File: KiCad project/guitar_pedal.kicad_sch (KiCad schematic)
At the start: 43 parts, among them J1 NMJ6HCD2, J2 NMJ6HCD2, J3 AVR-ISP-6, SW1 SW_SPST, SW2 SWITCH_3PDT, U1 ATmega1284-P, U2 L7805, U3 TL061, U4 TL061, Y1 Crystal 16MHz

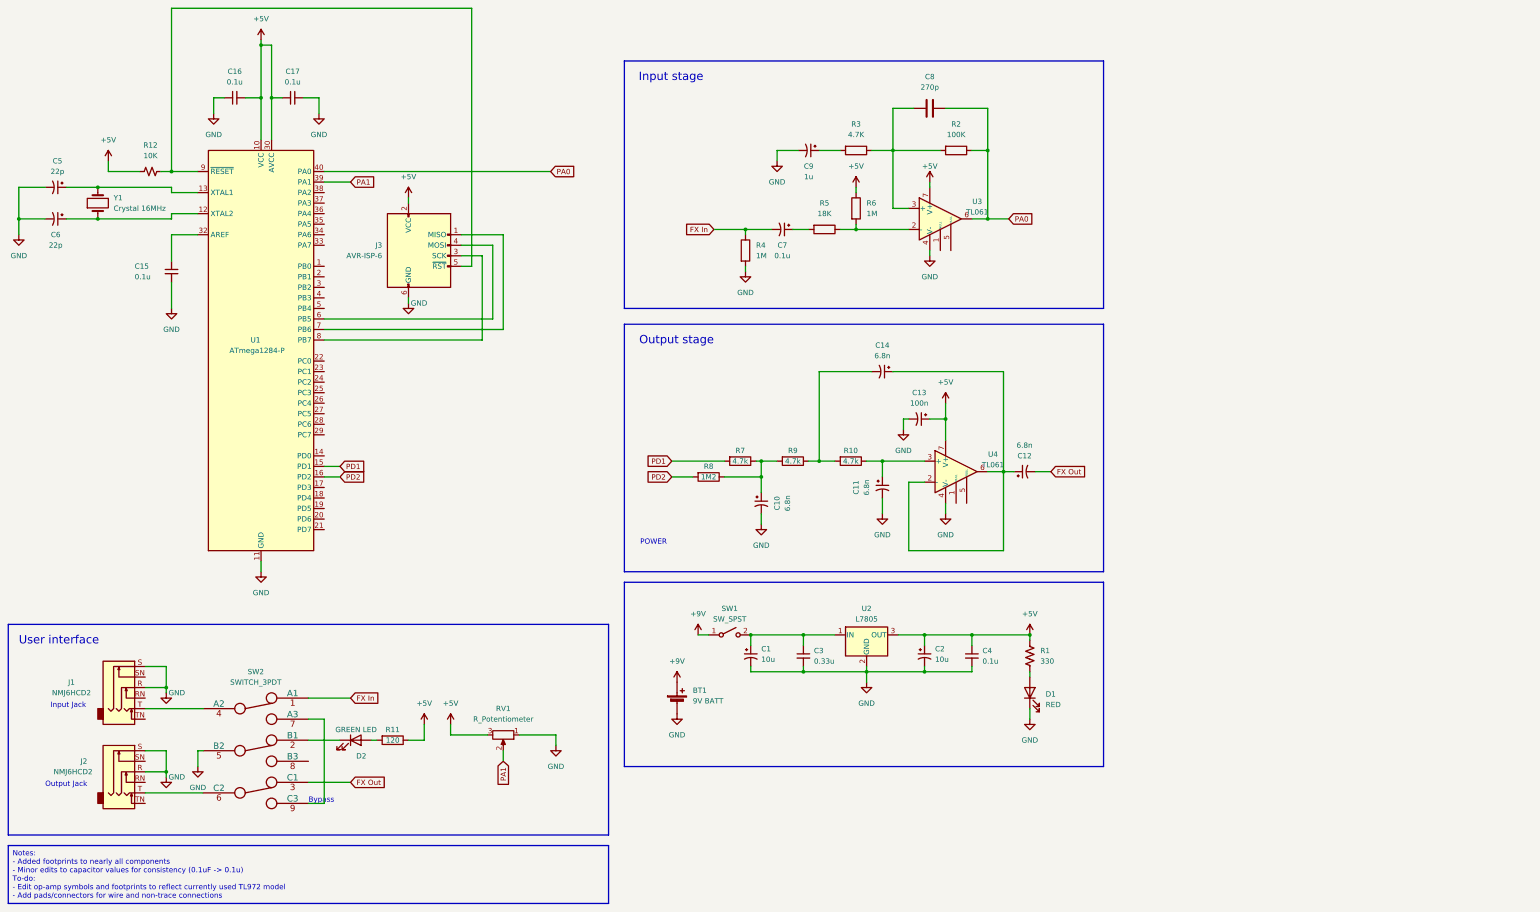
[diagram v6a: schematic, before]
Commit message: Updated schematic to match available components.
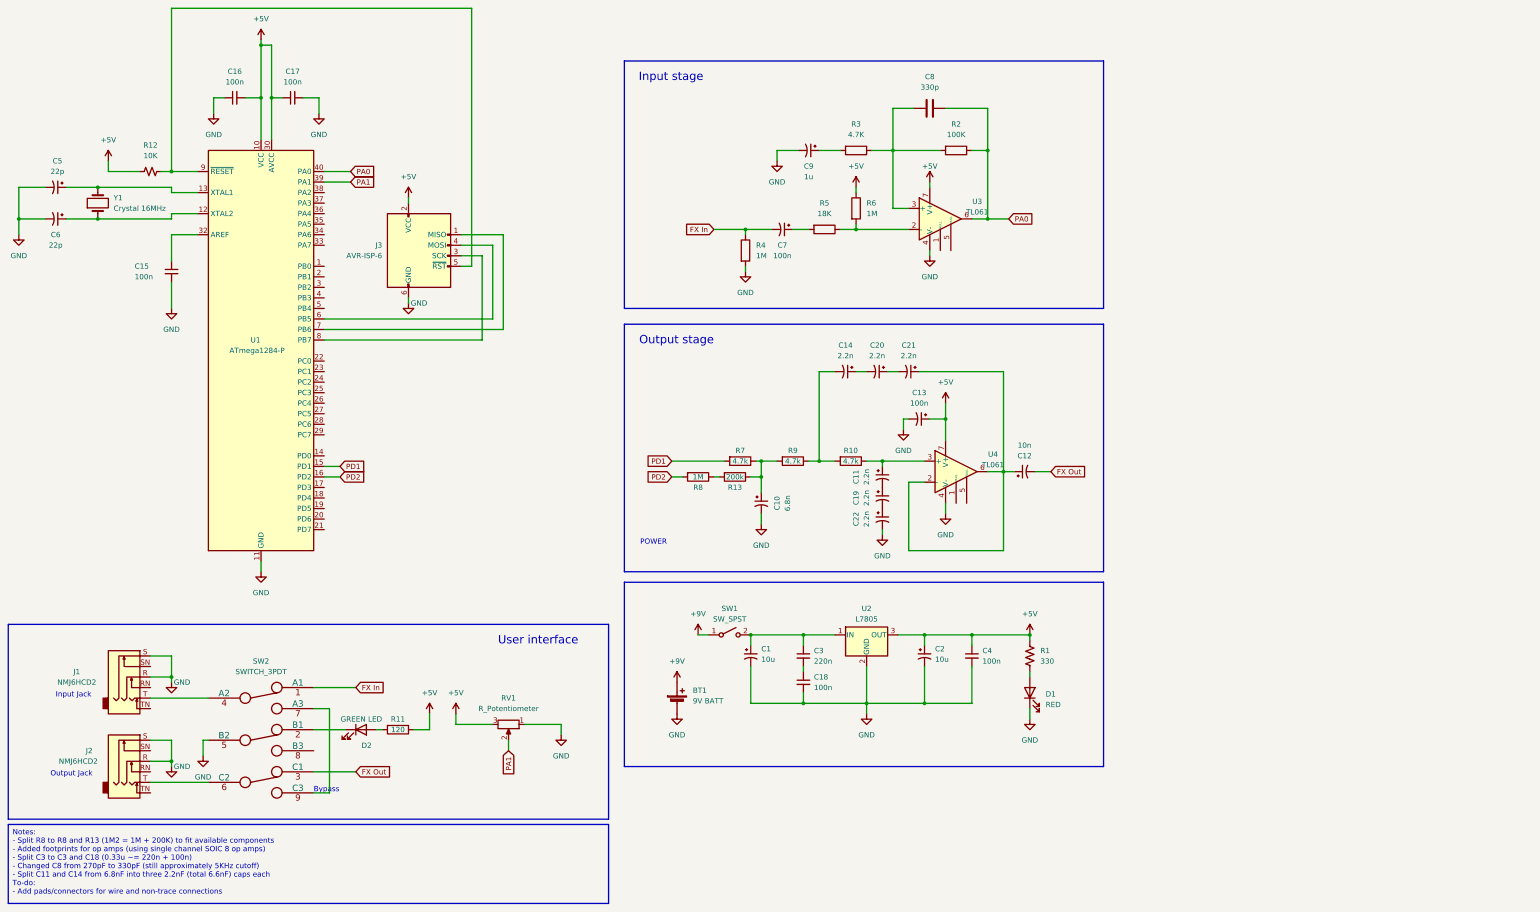
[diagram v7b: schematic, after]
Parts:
- added C18: 100n, Capacitor_SMD:C_1206_3216Metric, symbol Device:C_Small
- added C19, C20, C21, C22: 2.2n, Capacitor_SMD:C_1206_3216Metric, symbol Device:C_Polarized_Small_US
- added R13: 200k, Resistor_SMD:R_1206_3216Metric, symbol Device:R
- C11, C14: value 6.8n -> 2.2n
- C12: value 6.8n -> 10n
- C15, C16, C17, C4, C7: value 0.1u -> 100n
- C3: value 0.33u -> 220n
- C8: value 270p -> 330p
- R8: value 1M2 -> 1M
- U4: footprint (none) -> Package_SO:SOIC-8-1EP_3.9x4.9mm_P1.27mm_EP2.29x3mm
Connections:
- net GND: now also C18.2, C22.2; no longer C11.2, C3.2
- net at C10.1, R7.1, R9.2: now also R13.1; no longer R8.1
- net at C12.1, U4.2 (-), U4.6: now also C21.1; no longer C14.1
- new net: C14.1, C20.2
- new net: C20.1, C21.2
- new net: C11.2, C19.1
- new net: C19.2, C22.1
- new net: R13.2, R8.1
- new net: C18.1, C3.2
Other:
- moved on the sheet: C11, C14, D2, J1, J2, R11, R8, RV1, SW2

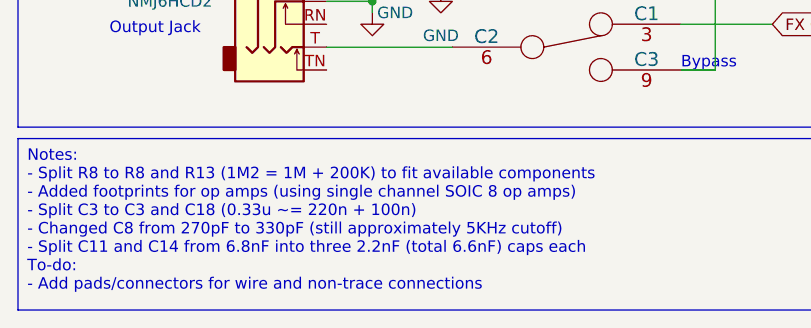
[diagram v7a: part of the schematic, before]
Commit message: Updates to PCB layout, most connections except ground/power added.
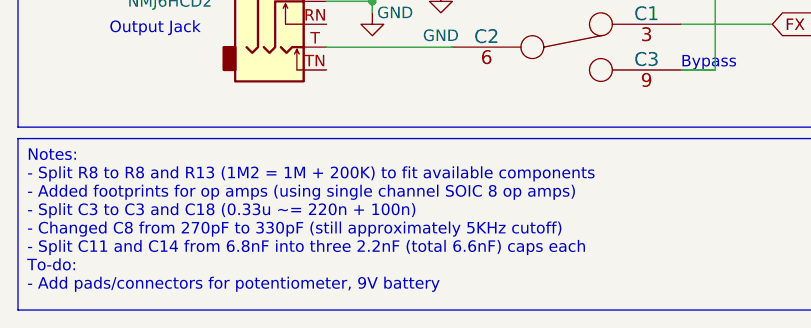
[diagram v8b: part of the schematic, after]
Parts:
- C1, C2: footprint Capacitor_SMD:CP_Elec_4x5.4 -> Capacitor_SMD:C_1206_3216Metric
- C9: footprint Capacitor_SMD:C_Elec_4x5.4 -> Capacitor_SMD:C_1206_3216Metric
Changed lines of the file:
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@@
     (fill (type none))
   )
-  (text_box "Notes:\n- Split R8 to R8 and R13 (1M2 = 1M + 200K) to fit available components\n- Added footprints for op amps (using single channel SOIC 8 op amps)\n- Split C3 to C3 and C18 (0.33u ~= 220n + 100n)\n- Changed C8 from 270pF to 330pF (still approximately 5KHz cutoff)\n- Split C11 and C14 from 6.8nF into three 2.2nF (total 6.6nF) caps each\nTo-do:\n- Add pads/connectors for wire and non-trace connections"
+  (text_box "Notes:\n- Split R8 to R8 and R13 (1M2 = 1M + 200K) to fit available components\n- Added footprints for op amps (using single channel SOIC 8 op amps)\n- Split C3 to C3 and C18 (0.33u ~= 220n + 100n)\n- Changed C8 from 270pF to 330pF (still approximately 5KHz cutoff)\n- Split C11 and C14 from 6.8nF into three 2.2nF (total 6.6nF) caps each\nTo-do:\n- Add pads/connectors for potentiometer, 9V battery"
     (at 20.32 214.63 0) (size 144.78 19.05)
     (stroke (width 0) (type default))
@@
       (effects (font (size 1.27 1.27)) (justify left))
     )
-    (property "Footprint" "Capacitor_SMD:CP_Elec_4x5.4" (at 241.3 173.99 0)
+    (property "Footprint" "Capacitor_SMD:C_1206_3216Metric" (at 241.3 173.99 0)
       (effects (font (size 1.27 1.27)) hide)
     )
@@
       (effects (font (size 1.27 1.27)) (justify left))
     )
-    (property "Footprint" "Capacitor_SMD:CP_Elec_4x5.4" (at 199.39 173.99 0)
+    (property "Footprint" "Capacitor_SMD:C_1206_3216Metric" (at 199.39 173.99 0)
       (effects (font (size 1.27 1.27)) hide)
     )
@@
       (effects (font (size 1.27 1.27)))
     )
-    (property "Footprint" "Capacitor_SMD:C_Elec_4x5.4" (at 213.36 52.07 0)
-      (effects (font (size 1.27 1.27)) hide)
-    )
+    (property "Footprint" "Capacitor_SMD:C_1206_3216Metric" (at 213.36 52.07 0)
+      (effects (font (size 1.27 1.27)) hide)
+    )
